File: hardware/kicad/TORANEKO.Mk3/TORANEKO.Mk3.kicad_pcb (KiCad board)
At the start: 2 copper layers, 40 x 64 mm, 90 parts, among them IC1 MP6551GQB-P, IC2 MP6551GQB-P, IC3 NCR321PASX, IC4 NCR321PASX, IC5 AS5047P-ATSM, IC6 STM32F411CEU6TR, IC7 AS5047P-ATSM, IC8 NCR321PASX, IC9 NCR321PASX, J1 Conn_01x02_Pin, J2 Conn_01x02_Pin, J3 Conn_01x02_Male, J4 Conn_01x02_Pin, J5 Conn_01x02_Pin, J6 Conn_02x03_Odd_Even, Q1 IRLML6402, Q5 IRLML6344, SW1 SW_Push, U1 LSM6DSRXTR, U2 LXDC55FAAA-203, U3 Encord, U4 Encord_B, U5 Encord, U6 Encord_B, Y1 CSTNE10M0G52Z000R0

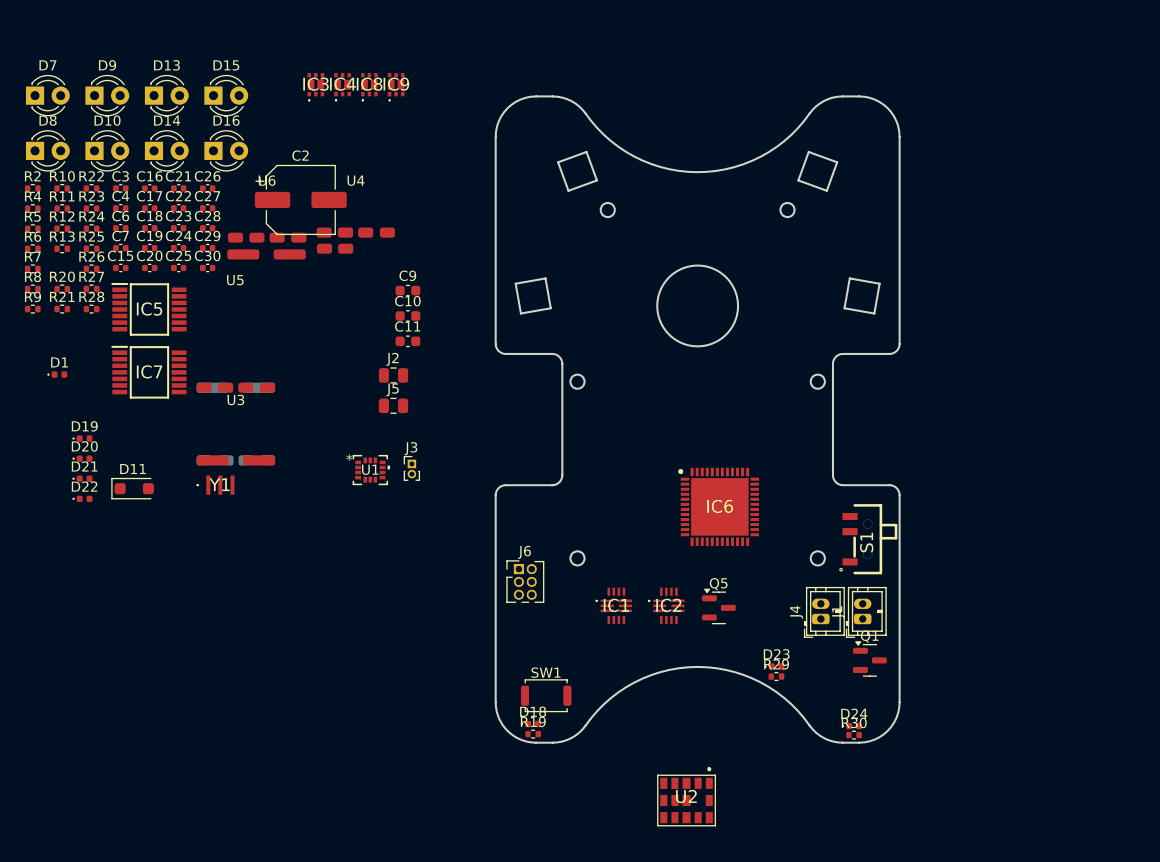
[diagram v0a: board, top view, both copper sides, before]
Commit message: Continue TORANEKO.Mk3 PCB layout and schematic update
- PCB layout progress (.kicad_pcb)
- Schematic updates (.kicad_sch)
- Change default via/pad size in project settings
- Ignore KiCad local history directory (.history/)

Co-Authored-By: Claude Opus 5.5 <noreply@anthropic.com>
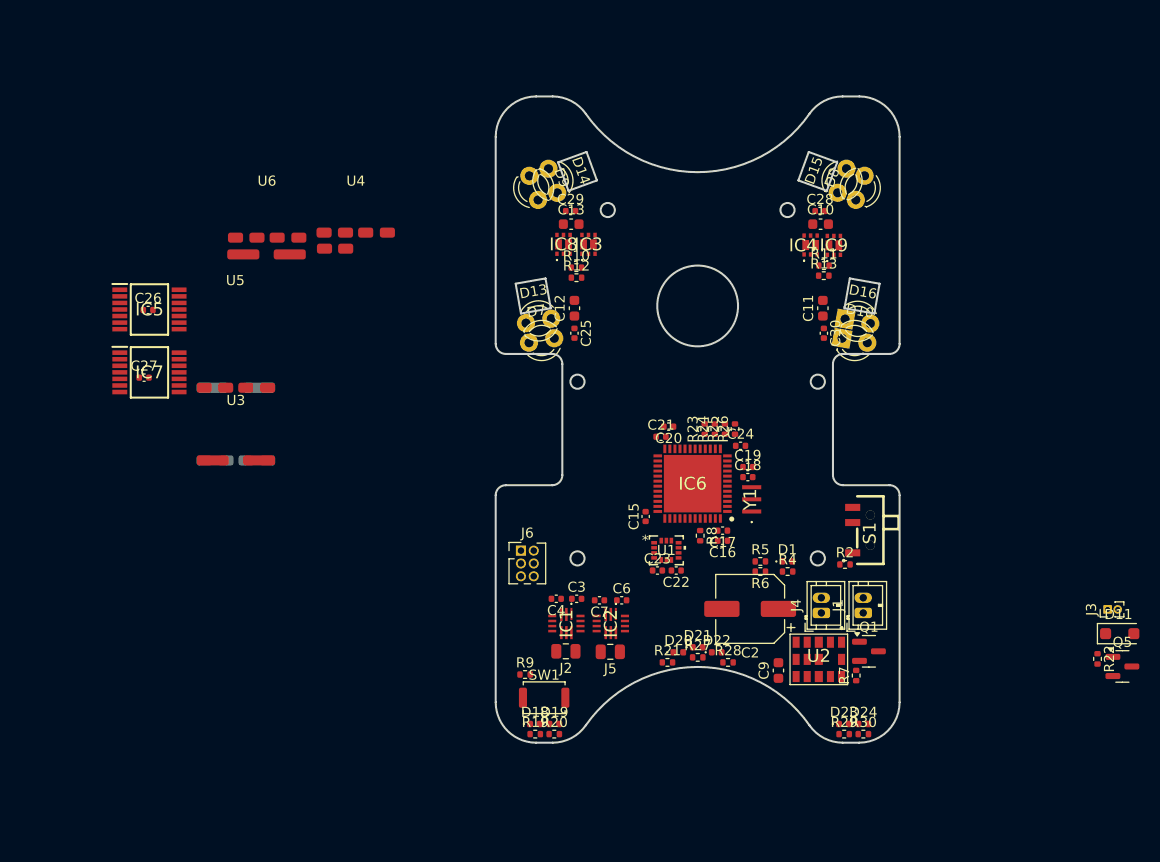
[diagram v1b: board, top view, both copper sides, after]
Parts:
- added C12: 47u, Capacitor_SMD:C_0603_1608Metric, F.Cu at (97.7, 55.0)
- added C13: 47u, Capacitor_SMD:C_0603_1608Metric, F.Cu at (97.4, 46.7)
- moved R22 110.0 mm to (149.5, 89.7), turned to -90 degrees
- moved D11 98.6 mm to (151.7, 87.2)
- moved R7 90.9 mm to (125.6, 91.4), turned to 90 degrees
- moved R2 88.6 mm to (124.5, 80.4)
- moved R4 82.9 mm to (118.8, 81.1)
- moved D8 81.4 mm to (125.6, 44.3), turned to 70 degrees
- moved R5 79.2 mm to (116.1, 80.1)
- moved R6 78.8 mm to (116.1, 81.1), turned to 180 degrees
- moved D10 76.3 mm to (124.2, 58.0), turned to -10 degrees
- moved R11 75.7 mm to (122.4, 50.8)
- moved R13 75.5 mm to (122.4, 51.8)
- moved D1 74.4 mm to (118.8, 80.1)
- moved R28 72.1 mm to (112.9, 90.1)
- moved R8 70.5 mm to (110.2, 77.5), turned to -90 degrees
- moved J3 70.4 mm to (150.5, 84.8), turned to 90 degrees
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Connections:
- R30 pad 2: unconnected-(R30-Pad2) -> GND
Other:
- board text added: "AS5047P side"
- board text added: "Bearing LF-630 (z>= 1.01mm above board)"
- board text added: "ENC_L board 6x0.6 (stands vertical)"
- board text added: "ENC_R board 6x0.6 (stands vertical)"
- board text added: "Fan motor MK06-45 (z>= 2.00mm above board)"
- board text added: "Fan motor mount (z>= 4.98mm above board)"
- board text added: "Import with the same origin/offset as the main board outline -> outlines overlap"
- board text added: "Motor (z>= 1.25mm above board)"
- board text added: "Pillar (on board)"
- board text added: "Pinion 11T (z>= 3.36mm above board)"
- board text added: "Shaft pin 3x6 (z>= 3.11mm above board)"
- board text added: "TORANEKO.Mk3 placement guide (same frame as main board outline DXF, from STEP v36)"
- board text added: "magnet axis"

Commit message: Continue TORANEKO.Mk3 PCB layout; add C14 to schematic
- PCB layout progress (.kicad_pcb)
- Schematic: add 47u capacitor C14
- Add preset track widths (0.1/0.3/0.5/1.0/2.0 mm) to board setup
- Ignore KiCad autosave index (#auto_saved_files#)

Co-Authored-By: Claude Opus 5.5 <noreply@anthropic.com>
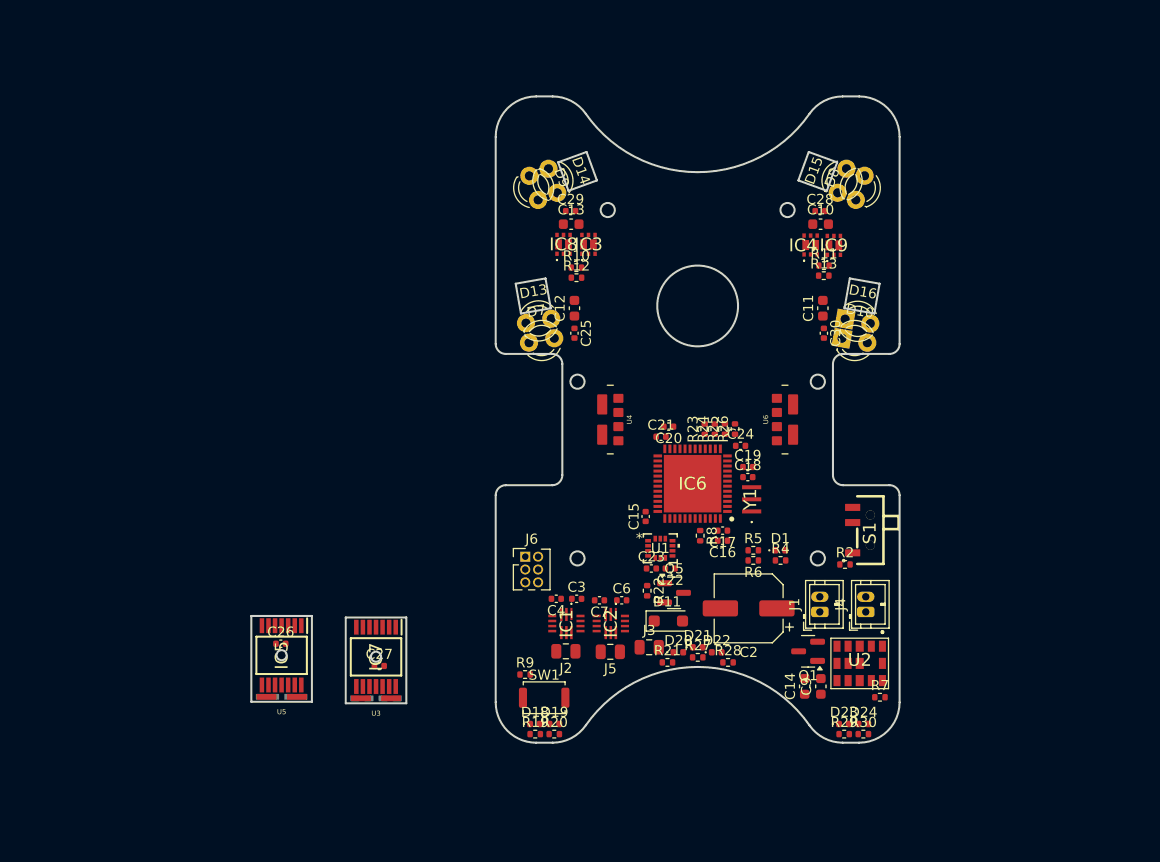
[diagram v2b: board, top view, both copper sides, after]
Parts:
- added C14: 47u, Capacitor_SMD:C_0603_1608Metric, F.Cu at (120.5, 92.5)
- J3: footprint Connector_PinHeader_1.00mm:PinHeader_1x02_P1.00mm_Vertical -> Capacitor_SMD:C_0805_2012Metric
- U3: footprint Encorder-WG:Encord_L -> TORANEKO_Encoder:TN_ENC_Edge
- U4: footprint Encorder-WG:Encord_B_L -> TORANEKO_Encoder:TN_ENC_Base
- U5: footprint Encorder-WG:Encord -> TORANEKO_Encoder:TN_ENC_Edge
- U6: footprint Encorder-WG:Encord_B -> TORANEKO_Encoder:TN_ENC_Base
- moved U6 56.3 mm to (118.5, 66.0), turned to -90 degrees
- moved J3 45.6 mm to (105.1, 88.6), turned to 0 degrees
- moved R22 45.1 mm to (104.9, 83.0)
- moved Q5 45.0 mm to (107.6, 83.2)
- moved D11 44.7 mm to (107.0, 86.0)
- moved U5 41.5 mm to (68.7, 94.0), turned to 180 degrees
- moved C27 36.8 mm to (78.4, 90.5)
- moved IC5 36.7 mm to (68.7, 89.4), turned to -90 degrees
- moved IC7 36.0 mm to (78.0, 89.5), turned to -90 degrees
- moved C26 35.6 mm to (68.6, 88.2)
- moved U4 34.2 mm to (101.2, 66.0), turned to 90 degrees
- moved U3 32.6 mm to (78.0, 94.2), turned to 180 degrees
- moved Q1 6.02 mm to (120.8, 89.0), turned to 180 degrees
- moved C9 4.49 mm to (122.1, 92.5)
- moved J4 4.40 mm to (126.5, 85.1)
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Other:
- board size 40 x 64 mm -> 64.2 x 64 mm

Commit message: Route TORANEKO.Mk3 PCB: add tracks, vias and a zone
- Add ~1034 track segments, 155 vias and 1 copper zone
- Update preset track widths (0.15/0.3/0.4/0.8/1.5 mm)
- Change default pad size to 4.0 x 4.0 mm (drill 0)

Co-Authored-By: Claude Opus 5.5 <noreply@anthropic.com>
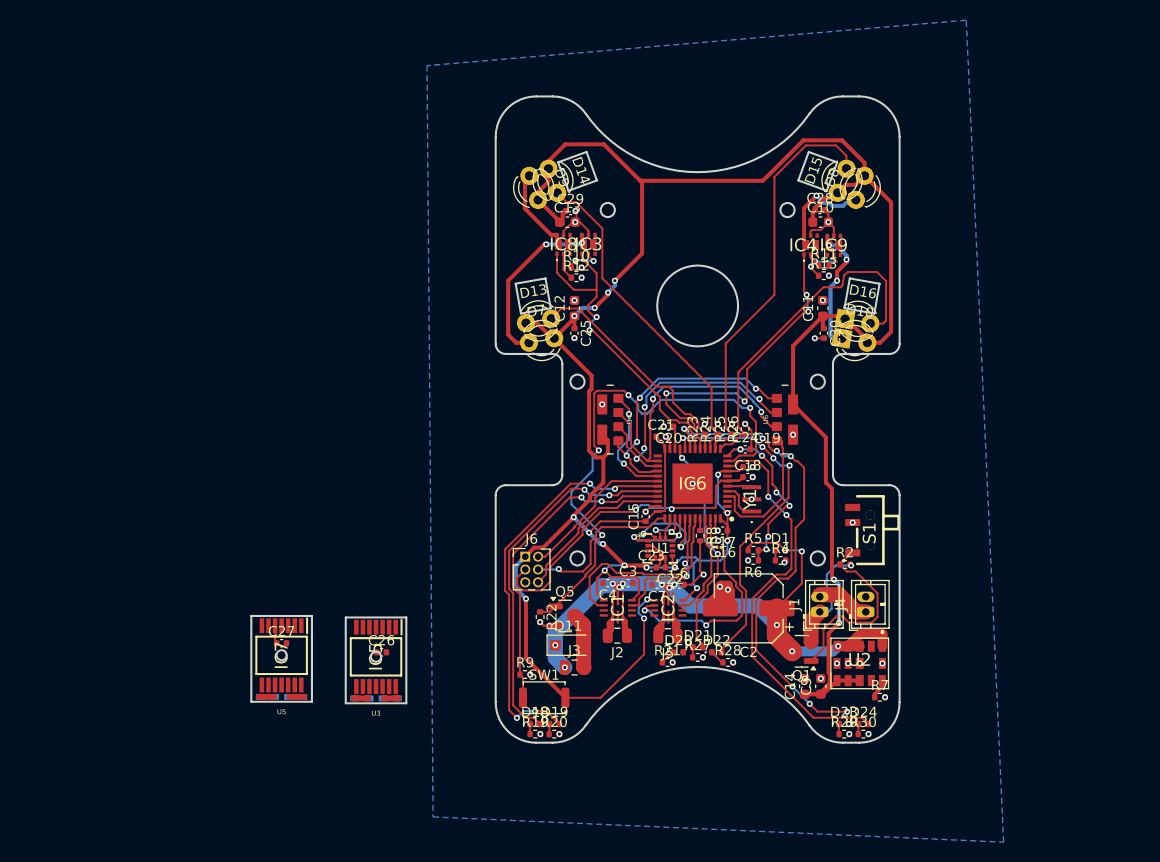
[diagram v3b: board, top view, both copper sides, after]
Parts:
- moved Q5 11.0 mm to (96.8, 85.5)
- moved R22 10.9 mm to (94.3, 85.6)
- moved D11 10.1 mm to (97.2, 88.4)
- moved C26 10.0 mm to (78.6, 89.1)
- moved C27 9.93 mm to (68.7, 88.2)
- moved IC5 9.35 mm to (78.0, 89.5)
- moved IC7 9.35 mm to (68.7, 89.4)
- moved J3 7.67 mm to (97.7, 90.6)
- moved C6 5.91 mm to (108.1, 82.4)
- moved IC2 5.91 mm to (107.0, 84.7)
- moved J5 5.91 mm to (107.0, 87.5)
- moved C7 5.91 mm to (105.9, 82.4)
- moved J2 5.33 mm to (102.0, 87.5)
- moved C3 5.33 mm to (103.0, 82.2)
- moved C4 5.33 mm to (101.0, 82.2)
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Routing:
- net +3.3V: track 0.00 -> 284.3 mm, vias 0 -> 20
- net VBAT: track 0.00 -> 73.9 mm, vias 0 -> 13
- net FunPWM: track 0.00 -> 52.9 mm, vias 0 -> 4
- net LED6: track 0.00 -> 49.3 mm, vias 0 -> 8
- net GND: track 0.00 -> 43.4 mm, vias 0 -> 47
- net LED2: track 0.00 -> 42.3 mm, vias 0 -> 4
- net Wallsen-3: track 0.00 -> 40.5 mm
- net LED7: track 0.00 -> 40.4 mm, vias 0 -> 2
- net LED1: track 0.00 -> 36.6 mm, vias 0 -> 2
- net LED5: track 0.00 -> 34.7 mm, vias 0 -> 4
- net Wallsen-4: track 0.00 -> 34.6 mm
- net NRST: track 0.00 -> 33.0 mm, vias 0 -> 2
- net WallLED-2: track 0.00 -> 33.0 mm, vias 0 -> 4
- net WallLED-1: track 0.00 -> 32.9 mm, vias 0 -> 2
- net Wallsen-2: track 0.00 -> 32.8 mm
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- added copper zone on B.Cu, net GND

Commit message: Continue TORANEKO.Mk3 PCB routing; relax clearances; re-export PDF
- Routing progress: 1034 -> 1246 track segments, 155 -> 185 vias
- Design rules: min clearance and copper-to-edge clearance 0.5 -> 0.2 mm
- Re-export schematic PDF

Co-Authored-By: Claude Opus 5.5 <noreply@anthropic.com>
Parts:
- C26, C27: moved to B.Cu
- moved IC7 17.0 mm to (85.5, 87.3), turned to 90 degrees
- moved U5 17.0 mm to (85.5, 91.9)
- moved C27 16.9 mm to (85.5, 87.3)
- moved IC5 2.36 mm to (78.0, 87.2), turned to 90 degrees
- moved U3 2.36 mm to (78.0, 91.8)
- moved C26 1.99 mm to (78.0, 87.2)
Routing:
- net LED3: track 0.00 -> 41.3 mm, vias 0 -> 6
- net GND: track 43.4 -> 71.1 mm, vias 47 -> 56
- net Net-(IC5-GND): track 0.00 -> 13.9 mm, vias 0 -> 1
- net Net-(IC7-GND): track 1.81 -> 15.0 mm, vias 0 -> 1
- net Net-(IC7-VDD): track 0.00 -> 10.3 mm, vias 0 -> 1
- net Net-(IC5-VDD): track 0.00 -> 9.62 mm, vias 0 -> 1
- net VBAT: track 73.9 -> 79.6 mm
- net Net-(IC7-MOSI): track 0.00 -> 5.15 mm, vias 0 -> 1
- net Net-(IC5-MOSI): track 0.00 -> 5.00 mm, vias 0 -> 1
- net Net-(IC7-MISO): track 0.00 -> 4.80 mm, vias 0 -> 1
- net Net-(IC5-MISO): track 0.00 -> 4.76 mm, vias 0 -> 1
- net Net-(IC7-CSN): track 0.00 -> 4.26 mm, vias 0 -> 1
- net Net-(IC5-CSN): track 0.00 -> 4.24 mm, vias 0 -> 1
- net Net-(IC7-CLK): track 0.00 -> 4.00 mm, vias 0 -> 1
- net Net-(IC5-CLK): track 0.00 -> 3.69 mm, vias 0 -> 1
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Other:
- board size 64.2 x 64 mm -> 54.9 x 64 mm
